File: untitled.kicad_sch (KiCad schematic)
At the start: 0 parts

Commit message: Power Section done + added backup lipo
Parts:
- added J10: Display, symbol Connector_Generic:Conn_01x04
- added J11: Rotary_Encoder, symbol Connector_Generic:Conn_01x05
- added J5: Temp, symbol Connector_Generic:Conn_01x03
- added J5: Temp2, symbol Connector_Generic:Conn_01x03
- added J5: Water_Level, symbol Connector_Generic:Conn_01x03
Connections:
- new net +3.3V: J10.2 (Pin_2), J11.2 (Pin_2), J5.2 (Pin_2), J5.2 (Pin_2), J5.2 (Pin_2)
- new net GND: J10.1 (Pin_1), J11.1 (Pin_1), J5.1 (Pin_1), J5.1 (Pin_1), J5.1 (Pin_1)
- new net ROTARY_CLK: J11.4 (Pin_4)
- new net ROTARY_DATA: J11.5 (Pin_5)
- new net ROT_SW: J11.3 (Pin_3)
- new net SCL: J10.4 (Pin_4)
- new net SDA: J10.3 (Pin_3)
- new net TEMP1_DATA: J5.3 (Pin_3)
- new net TEMP2_DATA: J5.3 (Pin_3)
- new net WATER_LEVEL_DATA: J5.3 (Pin_3)
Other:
- note added: "Sensors/Inputs"

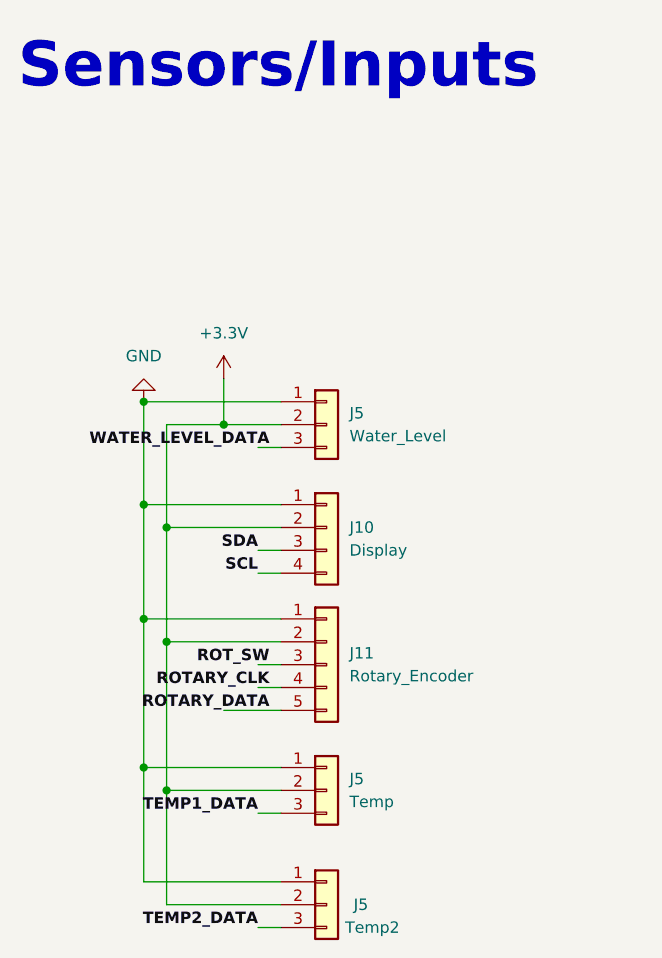
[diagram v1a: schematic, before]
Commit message: fixed R values
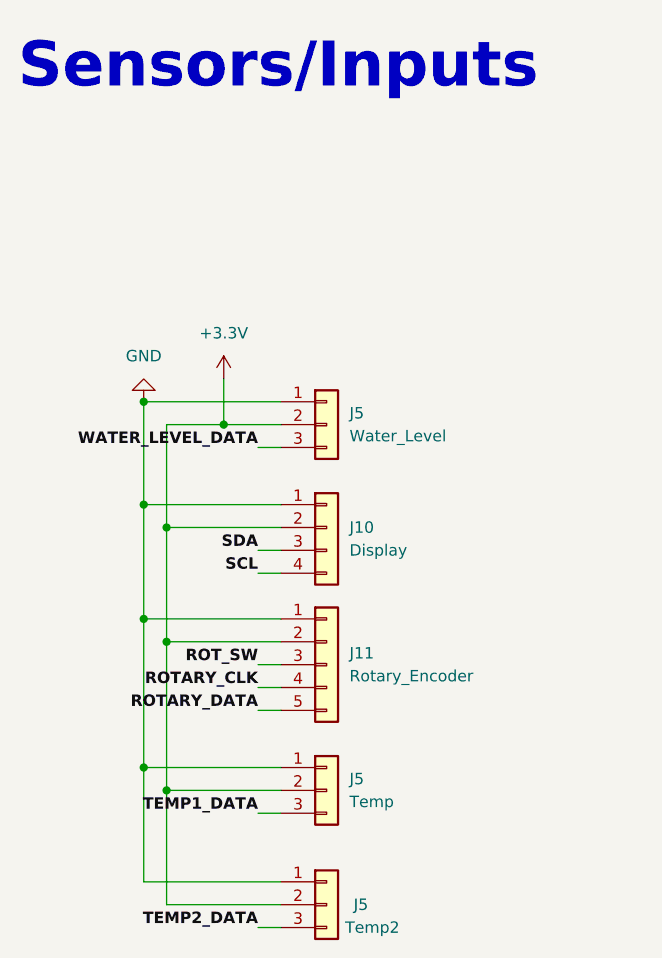
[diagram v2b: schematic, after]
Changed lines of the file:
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@@
-    (stroke (width 0) (type default))
-  )
-  (wire (pts (xy 147.32 118.11) (xy 144.78 118.11))
     (stroke (width 0) (type default))
   )
@@
     (stroke (width 0) (type default))
   )
+  (wire (pts (xy 144.78 120.65) (xy 147.32 120.65))
+    (stroke (width 0) (type default))
+  )
+  (wire (pts (xy 144.78 118.11) (xy 147.32 118.11))
+    (stroke (width 0) (type default))
+  )
   (wire (pts (xy 140.97 83.82) (xy 140.97 88.9))
     (stroke (width 0) (type default))
@@
     (stroke (width 0) (type default))
   )
-  (wire (pts (xy 147.32 120.65) (xy 140.97 120.65))
-    (stroke (width 0) (type default))
-  )
   (wire (pts (xy 132.08 110.49) (xy 132.08 97.79))
     (stroke (width 0) (type default))
   )
   (wire (pts (xy 147.32 129.54) (xy 134.62 129.54))
+    (stroke (width 0) (type default))
+  )
+  (wire (pts (xy 144.78 115.57) (xy 147.32 115.57))
     (stroke (width 0) (type default))
   )
@@
     (stroke (width 0) (type default))
   )
-  (wire (pts (xy 147.32 91.44) (xy 144.78 91.44))
+  (wire (pts (xy 144.78 91.44) (xy 147.32 91.44))
     (stroke (width 0) (type default))
   )
@@
   )
   (wire (pts (xy 147.32 144.78) (xy 144.78 144.78))
-    (stroke (width 0) (type default))
-  )
-  (wire (pts (xy 147.32 115.57) (xy 144.78 115.57))
     (stroke (width 0) (type default))
   )
@@
     (effects (font (face "KiCad Font") (size 5 5) (thickness 1) bold) (justify left bottom))
   )
-  (label "WATER_LEVEL_DATA" (at 146.05 91.44 180) (fields_autoplaced)
+  (label "WATER_LEVEL_DATA" (at 144.78 91.44 180) (fields_autoplaced)
     (effects (font (size 1.27 1.27) bold) (justify right bottom))
   )
@@
     (effects (font (size 1.27 1.27) bold) (justify right bottom))
   )
-  (label "ROT_SW" (at 146.05 115.57 180) (fields_autoplaced)
+  (label "ROT_SW" (at 144.78 115.57 180) (fields_autoplaced)
     (effects (font (size 1.27 1.27) bold) (justify right bottom))
   )
-  (label "ROTARY_CLK" (at 146.05 118.11 180) (fields_autoplaced)
+  (label "ROTARY_CLK" (at 144.78 118.11 180) (fields_autoplaced)
     (effects (font (size 1.27 1.27) bold) (justify right bottom))
   )
@@
     (effects (font (size 1.27 1.27) bold) (justify right bottom))
   )
-  (label "ROTARY_DATA" (at 146.05 120.65 180) (fields_autoplaced)
+  (label "ROTARY_DATA" (at 144.78 120.65 180) (fields_autoplaced)
     (effects (font (size 1.27 1.27) bold) (justify right bottom))
   )
